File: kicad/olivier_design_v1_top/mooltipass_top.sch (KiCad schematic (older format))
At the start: 30 parts, among them K1 CONN_3, P1 CONN_1, P2 CONN_1, P3 CONN_1, P4 CONN_1, U1 CON_STACK_9, U2 AT42QT2120

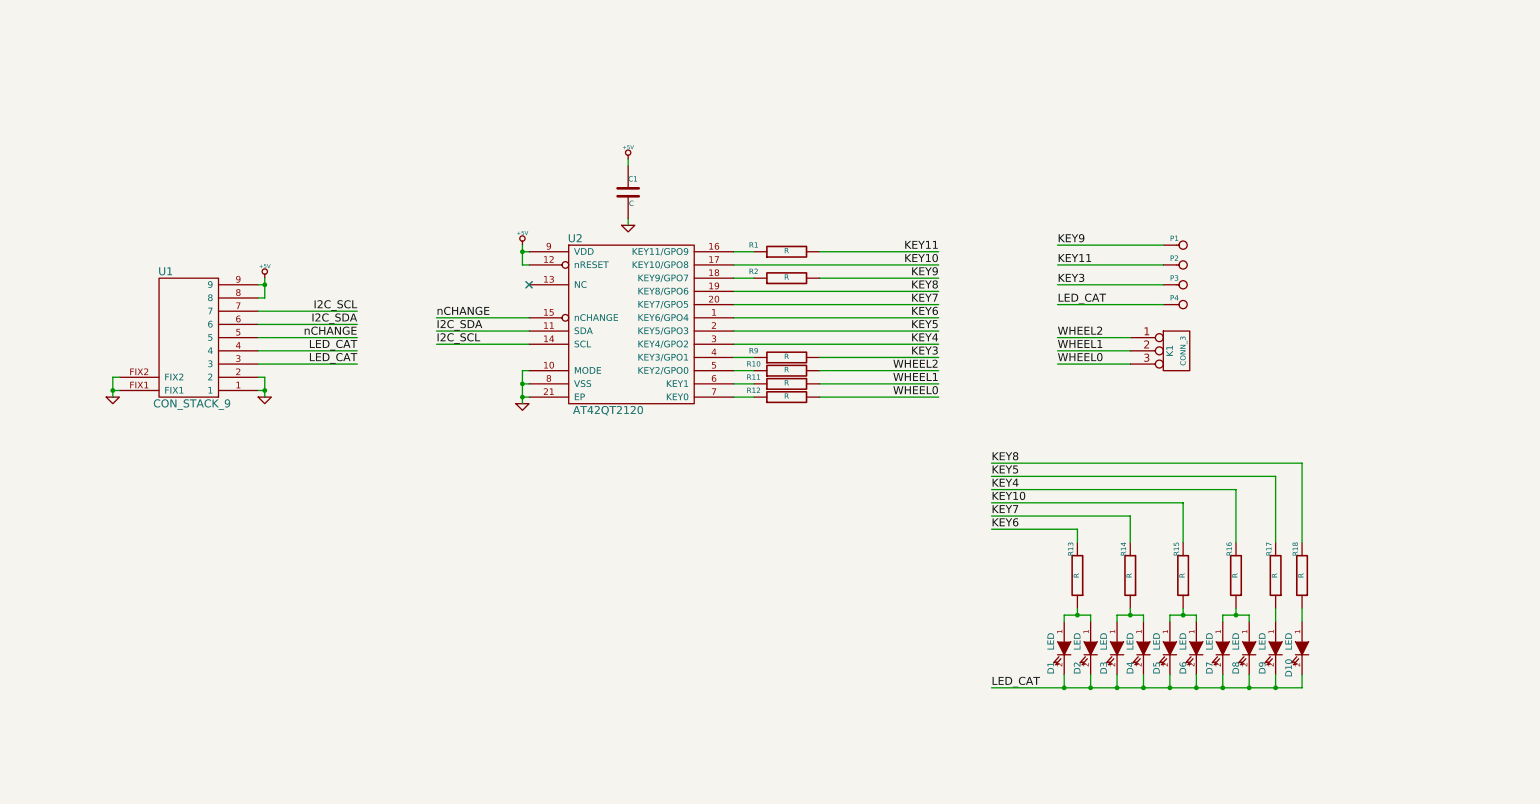
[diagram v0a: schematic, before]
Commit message: pwm code + updated schematics / smartcard designs
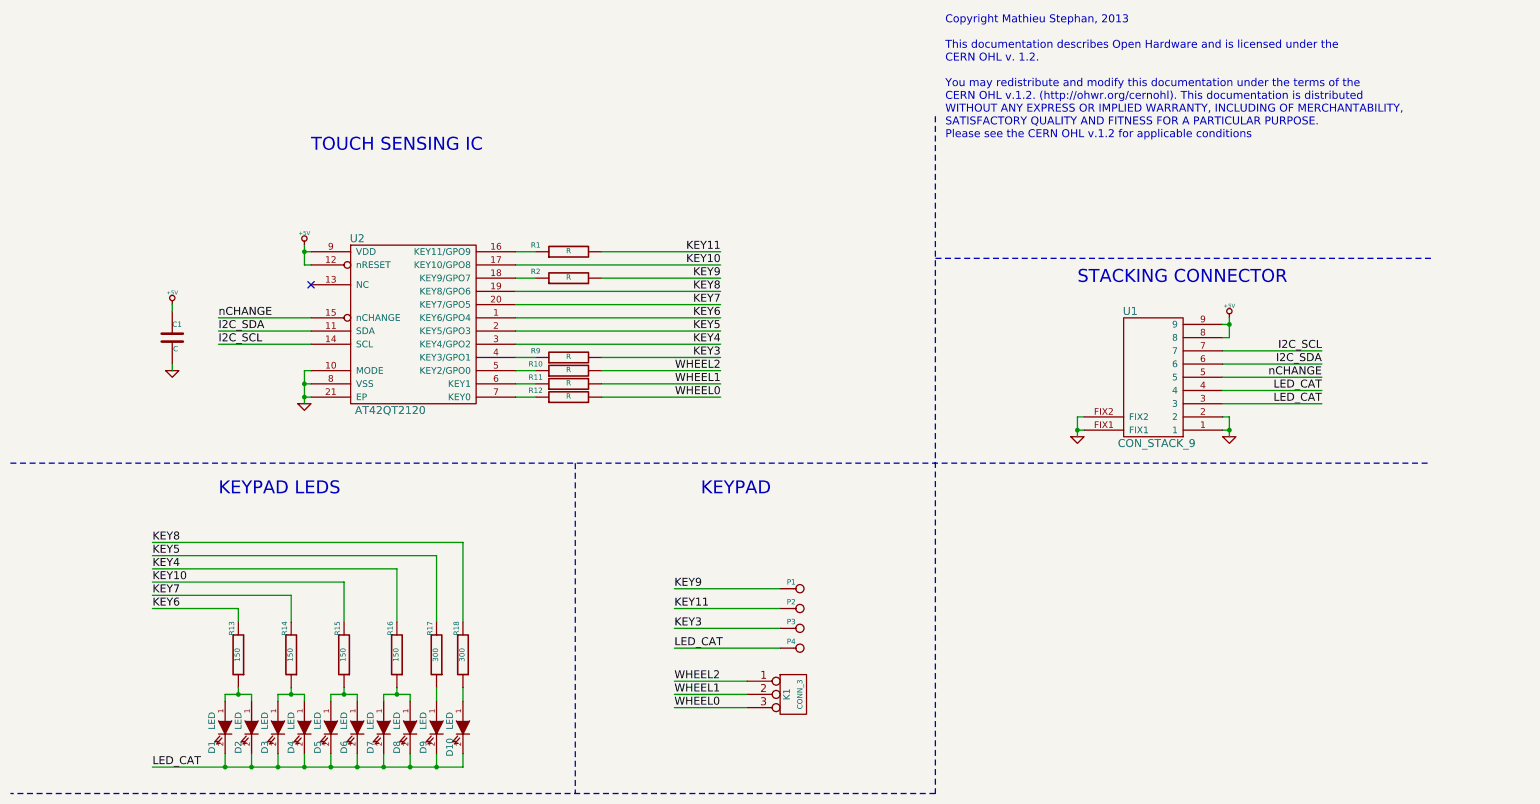
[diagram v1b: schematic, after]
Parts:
- R13, R14, R15, R16: value R -> 150
- R17, R18: value R -> 300
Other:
- note added: "Copyright Mathieu Stephan, 2013\n\nThis documentation describes Open Hardware and is licensed under the\nCERN OHL v. 1.2.\n\nYou may redistribute and modify this documentation under the terms of the\nCERN OHL v.1.2. (http://ohwr.org/cernohl). This documentation is distributed\nWITHOUT ANY EXPRESS OR IMPLIED WARRANTY, INCLUDING OF MERCHANTABILITY,\nSATISFACTORY QUALITY AND FITNESS FOR A PARTICULAR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"
- note added: "KEYPAD"
- note added: "KEYPAD LEDS"
- note added: "STACKING CONNECTOR"
- note added: "TOUCH SENSING IC"
- moved on the sheet: C1, D1, D10, D2, D3, D4, D5, D6, D7, D8, D9, K1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

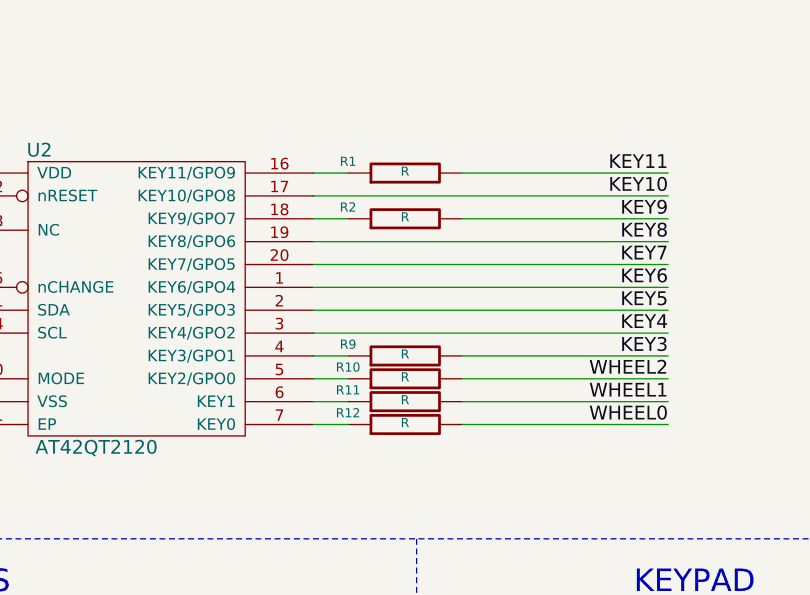
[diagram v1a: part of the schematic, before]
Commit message: update schematics + BoM
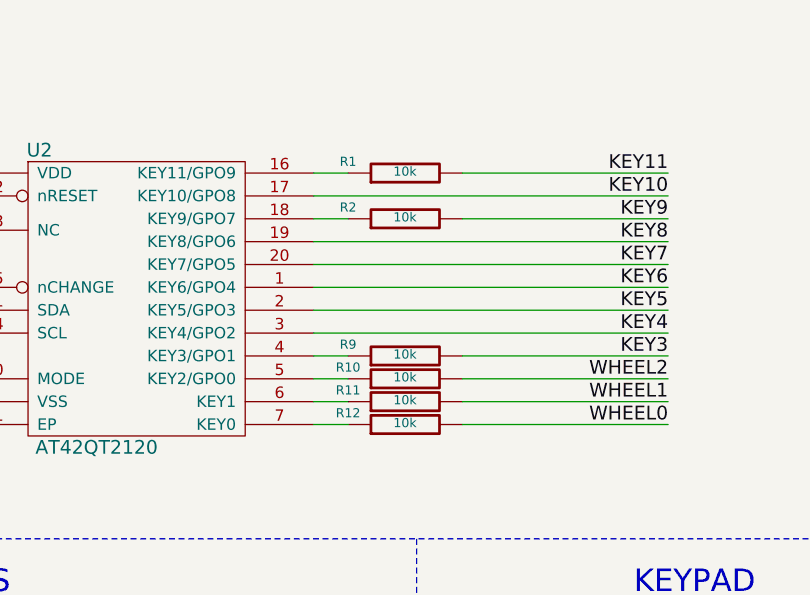
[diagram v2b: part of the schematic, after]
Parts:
- R1, R10, R11, R12, R2, R9: value R -> 10k
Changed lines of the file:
@@
 Sheet 1 1
 Title "M. Stephan - Top Touch Panel (Licensed under CERN OHL V1.2)"
-Date "12 apr 2014"
+Date "13 apr 2014"
 Rev "1"
 Comp ""
@@
 P 4700 2600
 F 0 "R12" V 4750 2850 40  0000 C CNN
-F 1 "R" V 4707 2601 40  0000 C CNN
+F 1 "10k" V 4707 2601 40  0000 C CNN
 F 2 "~" V 4630 2600 30  0000 C CNN
 F 3 "~" H 4700 2600 30  0000 C CNN
@@
 P 4700 2500
 F 0 "R11" V 4750 2750 40  0000 C CNN
-F 1 "R" V 4707 2501 40  0000 C CNN
+F 1 "10k" V 4707 2501 40  0000 C CNN
 F 2 "~" V 4630 2500 30  0000 C CNN
 F 3 "~" H 4700 2500 30  0000 C CNN
@@
 P 4700 2400
 F 0 "R10" V 4750 2650 40  0000 C CNN
-F 1 "R" V 4707 2401 40  0000 C CNN
+F 1 "10k" V 4707 2401 40  0000 C CNN
 F 2 "~" V 4630 2400 30  0000 C CNN
 F 3 "~" H 4700 2400 30  0000 C CNN
@@
 P 4700 2300
 F 0 "R9" V 4750 2550 40  0000 C CNN
-F 1 "R" V 4707 2301 40  0000 C CNN
+F 1 "10k" V 4707 2301 40  0000 C CNN
 F 2 "~" V 4630 2300 30  0000 C CNN
 F 3 "~" H 4700 2300 30  0000 C CNN
@@
 P 4700 1500
 F 0 "R1" V 4750 1750 40  0000 C CNN
-F 1 "R" V 4707 1501 40  0000 C CNN
+F 1 "10k" V 4707 1501 40  0000 C CNN
 F 2 "~" V 4630 1500 30  0000 C CNN
 F 3 "~" H 4700 1500 30  0000 C CNN
@@
 P 4700 1700
 F 0 "R2" V 4750 1950 40  0000 C CNN
-F 1 "R" V 4707 1701 40  0000 C CNN
+F 1 "10k" V 4707 1701 40  0000 C CNN
 F 2 "~" V 4630 1700 30  0000 C CNN
 F 3 "~" H 4700 1700 30  0000 C CNN

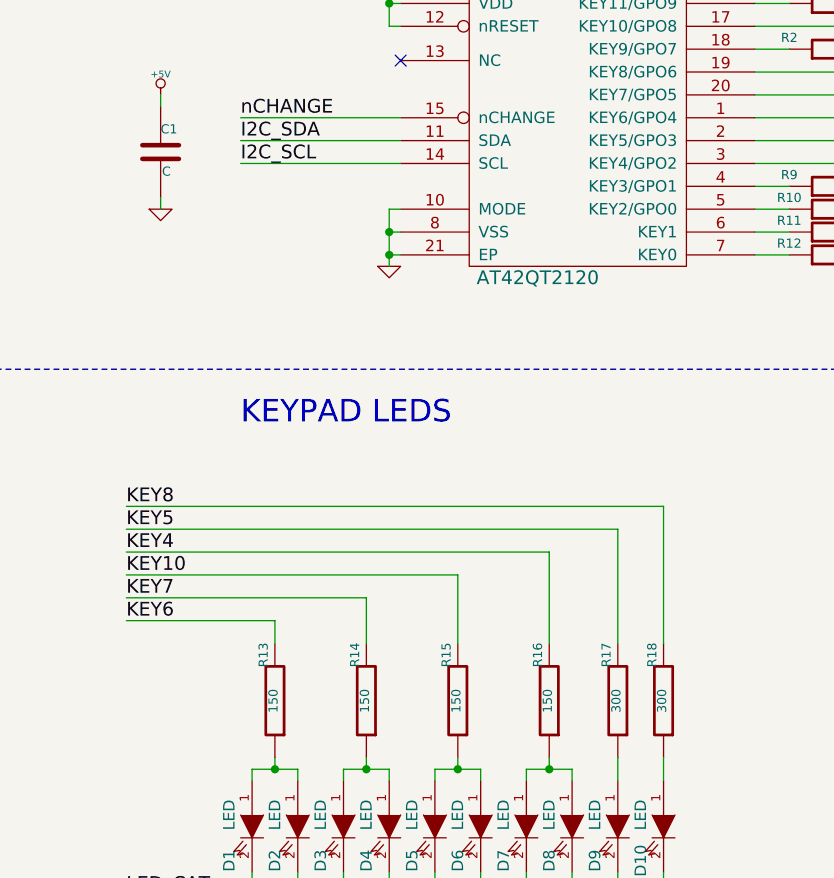
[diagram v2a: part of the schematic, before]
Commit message: updated resistor values
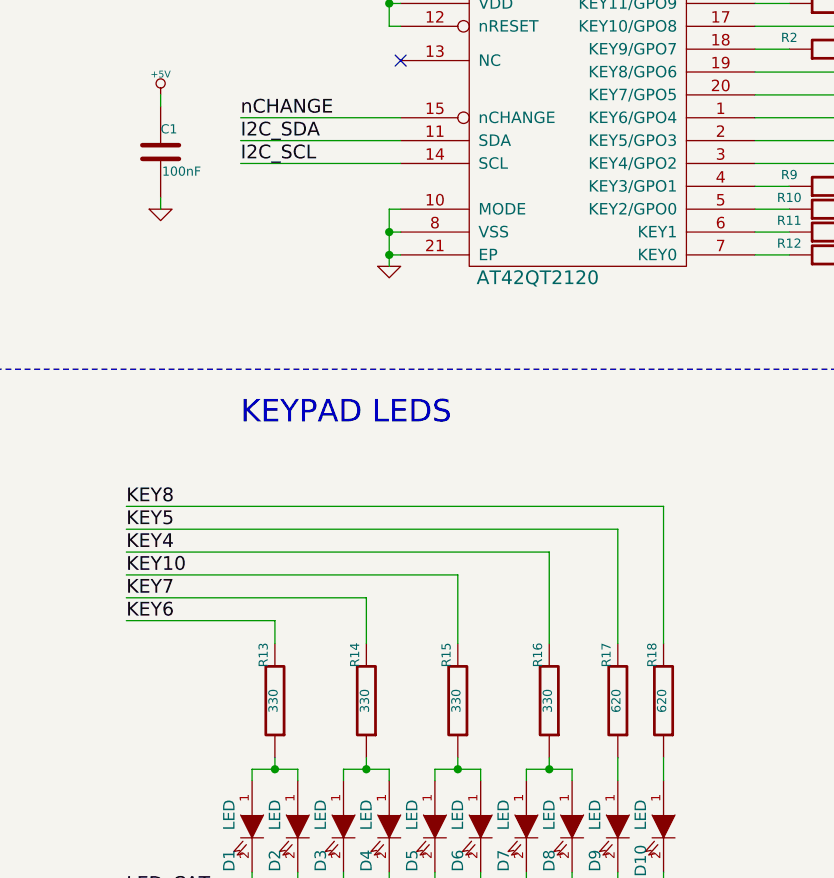
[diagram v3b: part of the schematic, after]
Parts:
- C1: value C -> 100nF
- R13, R14, R15, R16: value 150 -> 330
- R17, R18: value 300 -> 620
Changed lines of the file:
@@
 Sheet 1 1
 Title "M. Stephan - Top Touch Panel (Licensed under CERN OHL V1.2)"
-Date "13 apr 2014"
+Date "5 may 2014"
 Rev "1"
 Comp ""
@@
 P 1700 2150
 F 0 "C1" H 1700 2250 40  0000 L CNN
-F 1 "C" H 1706 2065 40  0000 L CNN
+F 1 "100nF" H 1706 2065 40  0000 L CNN
 F 2 "~" H 1738 2000 30  0000 C CNN
 F 3 "~" H 1700 2150 60  0000 C CNN
@@
 P 2200 4550
 F 0 "R13" V 2250 4350 40  0000 C CNN
-F 1 "150" V 2207 4551 40  0000 C CNN
+F 1 "330" V 2207 4551 40  0000 C CNN
 F 2 "~" V 2130 4550 30  0000 C CNN
 F 3 "~" H 2200 4550 30  0000 C CNN
@@
 P 2600 4550
 F 0 "R14" V 2650 4350 40  0000 C CNN
-F 1 "150" V 2607 4551 40  0000 C CNN
+F 1 "330" V 2607 4551 40  0000 C CNN
 F 2 "~" V 2530 4550 30  0000 C CNN
 F 3 "~" H 2600 4550 30  0000 C CNN
@@
 P 3000 4550
 F 0 "R15" V 3050 4350 40  0000 C CNN
-F 1 "150" V 3007 4551 40  0000 C CNN
+F 1 "330" V 3007 4551 40  0000 C CNN
 F 2 "~" V 2930 4550 30  0000 C CNN
 F 3 "~" H 3000 4550 30  0000 C CNN
@@
 P 3400 4550
 F 0 "R16" V 3450 4350 40  0000 C CNN
-F 1 "150" V 3407 4551 40  0000 C CNN
+F 1 "330" V 3407 4551 40  0000 C CNN
 F 2 "~" V 3330 4550 30  0000 C CNN
 F 3 "~" H 3400 4550 30  0000 C CNN
@@
 P 3700 4550
 F 0 "R17" V 3750 4350 40  0000 C CNN
-F 1 "300" V 3707 4551 40  0000 C CNN
+F 1 "620" V 3707 4551 40  0000 C CNN
 F 2 "~" V 3630 4550 30  0000 C CNN
 F 3 "~" H 3700 4550 30  0000 C CNN
@@
 P 3900 4550
 F 0 "R18" V 3950 4350 40  0000 C CNN
-F 1 "300" V 3907 4551 40  0000 C CNN
+F 1 "620" V 3907 4551 40  0000 C CNN
 F 2 "~" V 3830 4550 30  0000 C CNN
 F 3 "~" H 3900 4550 30  0000 C CNN

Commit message: update top gerbers
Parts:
- R13, R14, R15, R16: value 330 -> 390
- R17, R18: value 620 -> 750
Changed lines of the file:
@@
 LIBS:contrib
 LIBS:valves
-LIBS:limpkins_lib
 LIBS:mooltipass_top-cache
 EELAYER 27 0
@@
 encoding utf-8
 Sheet 1 1
-Title "M. Stephan - Top Touch Panel (Licensed under CERN OHL V1.2)"
-Date "5 may 2014"
+Title "M. Stephan - Mooltipass Touch Panel (Licensed under CERN OHL V1.2)"
+Date "21 jun 2014"
 Rev "1"
 Comp ""
@@
 P 2200 4550
 F 0 "R13" V 2250 4350 40  0000 C CNN
-F 1 "330" V 2207 4551 40  0000 C CNN
+F 1 "390" V 2207 4551 40  0000 C CNN
 F 2 "~" V 2130 4550 30  0000 C CNN
 F 3 "~" H 2200 4550 30  0000 C CNN
@@
 P 2600 4550
 F 0 "R14" V 2650 4350 40  0000 C CNN
-F 1 "330" V 2607 4551 40  0000 C CNN
+F 1 "390" V 2607 4551 40  0000 C CNN
 F 2 "~" V 2530 4550 30  0000 C CNN
 F 3 "~" H 2600 4550 30  0000 C CNN
@@
 P 3000 4550
 F 0 "R15" V 3050 4350 40  0000 C CNN
-F 1 "330" V 3007 4551 40  0000 C CNN
+F 1 "390" V 3007 4551 40  0000 C CNN
 F 2 "~" V 2930 4550 30  0000 C CNN
 F 3 "~" H 3000 4550 30  0000 C CNN
@@
 P 3400 4550
 F 0 "R16" V 3450 4350 40  0000 C CNN
-F 1 "330" V 3407 4551 40  0000 C CNN
+F 1 "390" V 3407 4551 40  0000 C CNN
 F 2 "~" V 3330 4550 30  0000 C CNN
 F 3 "~" H 3400 4550 30  0000 C CNN
@@
 P 3700 4550
 F 0 "R17" V 3750 4350 40  0000 C CNN
-F 1 "620" V 3707 4551 40  0000 C CNN
+F 1 "750" V 3707 4551 40  0000 C CNN
 F 2 "~" V 3630 4550 30  0000 C CNN
 F 3 "~" H 3700 4550 30  0000 C CNN
@@
 P 3900 4550
 F 0 "R18" V 3950 4350 40  0000 C CNN
-F 1 "620" V 3907 4551 40  0000 C CNN
+F 1 "750" V 3907 4551 40  0000 C CNN
 F 2 "~" V 3830 4550 30  0000 C CNN
 F 3 "~" H 3900 4550 30  0000 C CNN

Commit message: update top PCB
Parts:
- R10, R11, R12, R9: value 10k -> 4k7
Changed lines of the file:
@@
 Sheet 1 1
 Title "M. Stephan - Mooltipass Touch Panel (Licensed under CERN OHL V1.2)"
-Date "21 jun 2014"
+Date "2 aug 2014"
 Rev "1"
 Comp ""
@@
 P 4700 2600
 F 0 "R12" V 4750 2850 40  0000 C CNN
-F 1 "10k" V 4707 2601 40  0000 C CNN
+F 1 "4k7" V 4707 2601 40  0000 C CNN
 F 2 "~" V 4630 2600 30  0000 C CNN
 F 3 "~" H 4700 2600 30  0000 C CNN
@@
 P 4700 2500
 F 0 "R11" V 4750 2750 40  0000 C CNN
-F 1 "10k" V 4707 2501 40  0000 C CNN
+F 1 "4k7" V 4707 2501 40  0000 C CNN
 F 2 "~" V 4630 2500 30  0000 C CNN
 F 3 "~" H 4700 2500 30  0000 C CNN
@@
 P 4700 2400
 F 0 "R10" V 4750 2650 40  0000 C CNN
-F 1 "10k" V 4707 2401 40  0000 C CNN
+F 1 "4k7" V 4707 2401 40  0000 C CNN
 F 2 "~" V 4630 2400 30  0000 C CNN
 F 3 "~" H 4700 2400 30  0000 C CNN
@@
 P 4700 2300
 F 0 "R9" V 4750 2550 40  0000 C CNN
-F 1 "10k" V 4707 2301 40  0000 C CNN
+F 1 "4k7" V 4707 2301 40  0000 C CNN
 F 2 "~" V 4630 2300 30  0000 C CNN
 F 3 "~" H 4700 2300 30  0000 C CNN

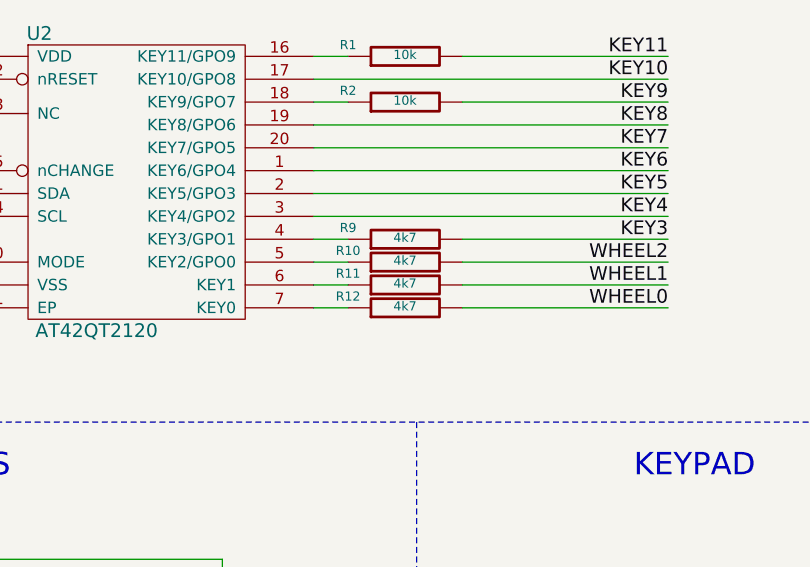
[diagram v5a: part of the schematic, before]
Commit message: 10k touch resistors, slots added on gerbers
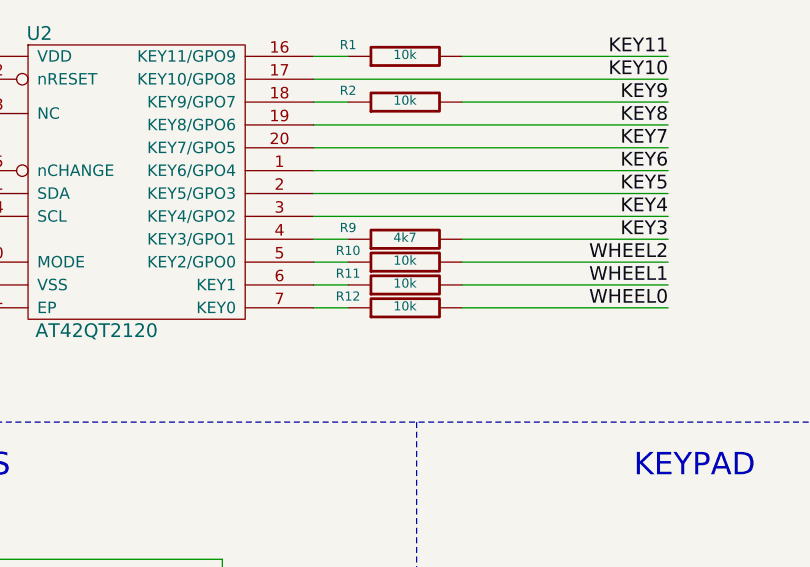
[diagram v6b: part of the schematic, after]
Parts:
- R10, R11, R12: value 4k7 -> 10k
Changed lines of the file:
@@
 Sheet 1 1
 Title "M. Stephan - Mooltipass Touch Panel (Licensed under CERN OHL V1.2)"
-Date "2 aug 2014"
+Date "15 feb 2015"
 Rev "1"
 Comp ""
@@
 P 4700 2600
 F 0 "R12" V 4750 2850 40  0000 C CNN
-F 1 "4k7" V 4707 2601 40  0000 C CNN
+F 1 "10k" V 4707 2601 40  0000 C CNN
 F 2 "~" V 4630 2600 30  0000 C CNN
 F 3 "~" H 4700 2600 30  0000 C CNN
@@
 P 4700 2500
 F 0 "R11" V 4750 2750 40  0000 C CNN
-F 1 "4k7" V 4707 2501 40  0000 C CNN
+F 1 "10k" V 4707 2501 40  0000 C CNN
 F 2 "~" V 4630 2500 30  0000 C CNN
 F 3 "~" H 4700 2500 30  0000 C CNN
@@
 P 4700 2400
 F 0 "R10" V 4750 2650 40  0000 C CNN
-F 1 "4k7" V 4707 2401 40  0000 C CNN
+F 1 "10k" V 4707 2401 40  0000 C CNN
 F 2 "~" V 4630 2400 30  0000 C CNN
 F 3 "~" H 4700 2400 30  0000 C CNN
